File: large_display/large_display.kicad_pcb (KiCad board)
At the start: 2 copper layers, 128 parts, among them J1 Conn_01x11, J2 Conn_01x11, U1 TLC5940PWP

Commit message: routing: first pass done
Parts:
- removed R2: R, Resistor_SMD:R_0805_2012Metric_Pad1.15x1.40mm_HandSolder
- added REF**: MountingHole_3.2mm_M3, MountingHole:MountingHole_3.2mm_M3, F.Cu at (138.4, 146.8)
- added REF**: MountingHole_3.2mm_M3, MountingHole:MountingHole_3.2mm_M3, F.Cu at (54.0, 146.0)
- added REF**: MountingHole_3.2mm_M3, MountingHole:MountingHole_3.2mm_M3, F.Cu at (138.2, 53.8)
- added REF**: MountingHole_3.2mm_M3, MountingHole:MountingHole_3.2mm_M3, F.Cu at (53.7, 53.7)
- moved R35 18.8 mm to (120.8, 138.6)
- moved R1 17.2 mm to (138.0, 131.4)
- moved Dk5 17.2 mm to (100.5, 129.0)
- moved U1 17.1 mm to (131.9, 132.8)
- moved C1 17.1 mm to (134.5, 126.0)
- moved Dk4 17.1 mm to (97.3, 118.3)
- moved Dk2 17.0 mm to (98.9, 123.7)
- moved Dd5 16.9 mm to (97.4, 146.2)
- moved Da6 16.9 mm to (92.6, 54.3)
- moved Dd7 16.8 mm to (71.9, 146.2)
- moved De7 16.8 mm to (60.4, 135.1)
- moved Db5 16.8 mm to (116.3, 65.2)
- moved Dd2 16.8 mm to (91.0, 146.2)
- moved DL2 16.8 mm to (87.3, 116.9)
- moved DL5 16.8 mm to (87.7, 111.7)
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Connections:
- Df7 pad 1: Net-(Df7-Pad1) -> Net-(Df4-Pad1)
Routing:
- net Vdrive: track 0.00 -> 494.7 mm, vias 0 -> 22
- net Net-(Df4-Pad1): track 0.00 -> 148.1 mm, vias 0 -> 2
- net Net-(Da4-Pad1): track 0.00 -> 134.8 mm, vias 0 -> 6
- net Net-(J1-Pad7): track 0.00 -> 132.7 mm, vias 0 -> 2
- net Net-(Dg2-Pad1): track 0.00 -> 126.5 mm, vias 0 -> 4
- net Net-(Dn2-Pad1): track 0.00 -> 126.1 mm, vias 0 -> 6
- net Net-(J1-Pad8): track 0.00 -> 125.0 mm, vias 0 -> 2
- net VCC: track 0.00 -> 119.1 mm, vias 0 -> 4
- net Net-(J1-Pad6): track 0.00 -> 119.0 mm, vias 0 -> 2
- net Net-(J1-Pad5): track 0.00 -> 118.1 mm, vias 0 -> 2
- net Net-(J1-Pad3): track 0.00 -> 116.5 mm
- net Net-(J1-Pad2): track 0.00 -> 115.2 mm, vias 0 -> 2
- net Net-(J1-Pad1): track 0.00 -> 114.7 mm, vias 0 -> 2
- net Net-(J1-Pad4): track 0.00 -> 113.6 mm, vias 0 -> 2
- net Net-(Dh3-Pad1): track 0.00 -> 110.0 mm, vias 0 -> 6
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- added copper zone on B.Cu, net GND
- added copper zone on F.Cu, net GND
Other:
- board outline added: 92 x 100 mm
- net class Default: clearance 0.2 -> 0.16; trace_width 0.25 -> 0.2
- net class HiPower added: clearance 0.16, trace_width 0.6, via_dia 1, via_drill 0.5
- net class Lowpower added: clearance 0.16, trace_width 0.5, via_dia 1, via_drill 0.5
- rule trace_clearance: 0.2 -> 0.16
- board text added: "VLED GND VCC SDO SCK"

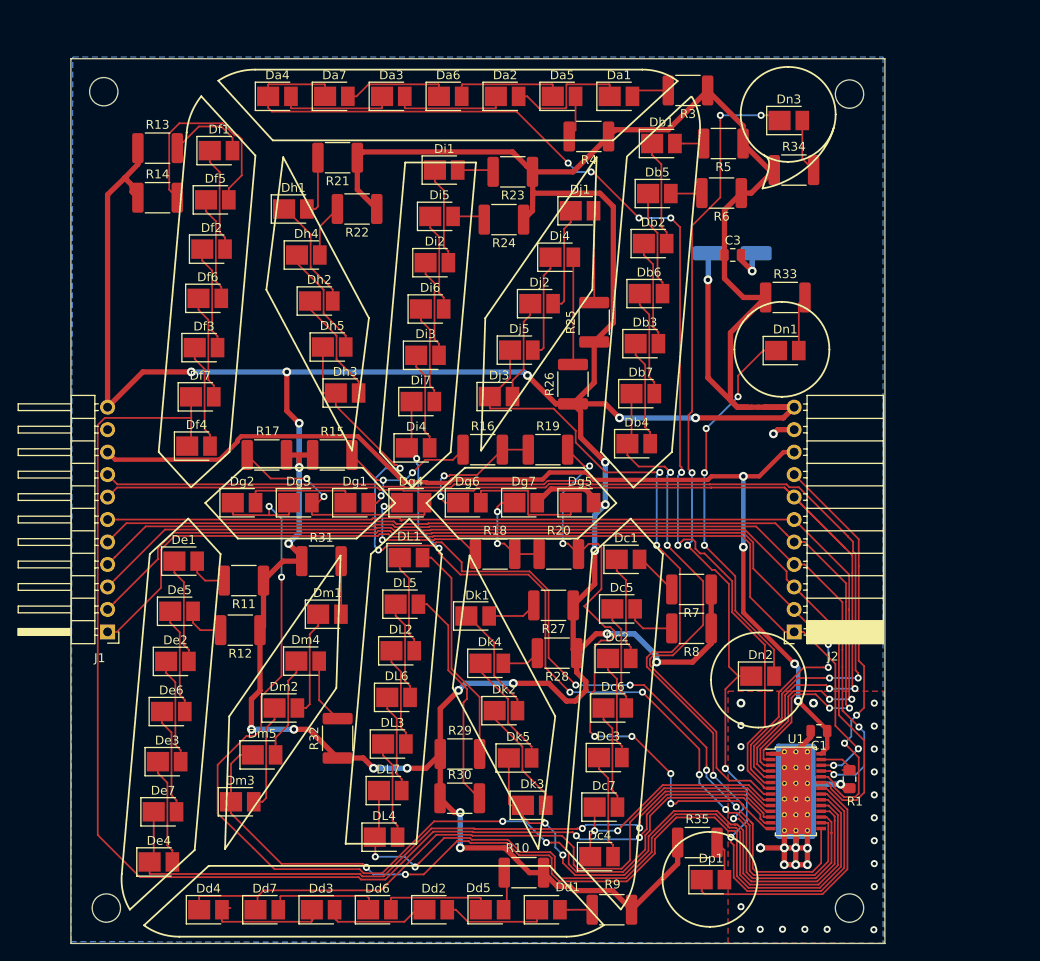
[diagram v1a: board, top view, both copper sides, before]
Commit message: first rev of layout done, text added to back silkscreen
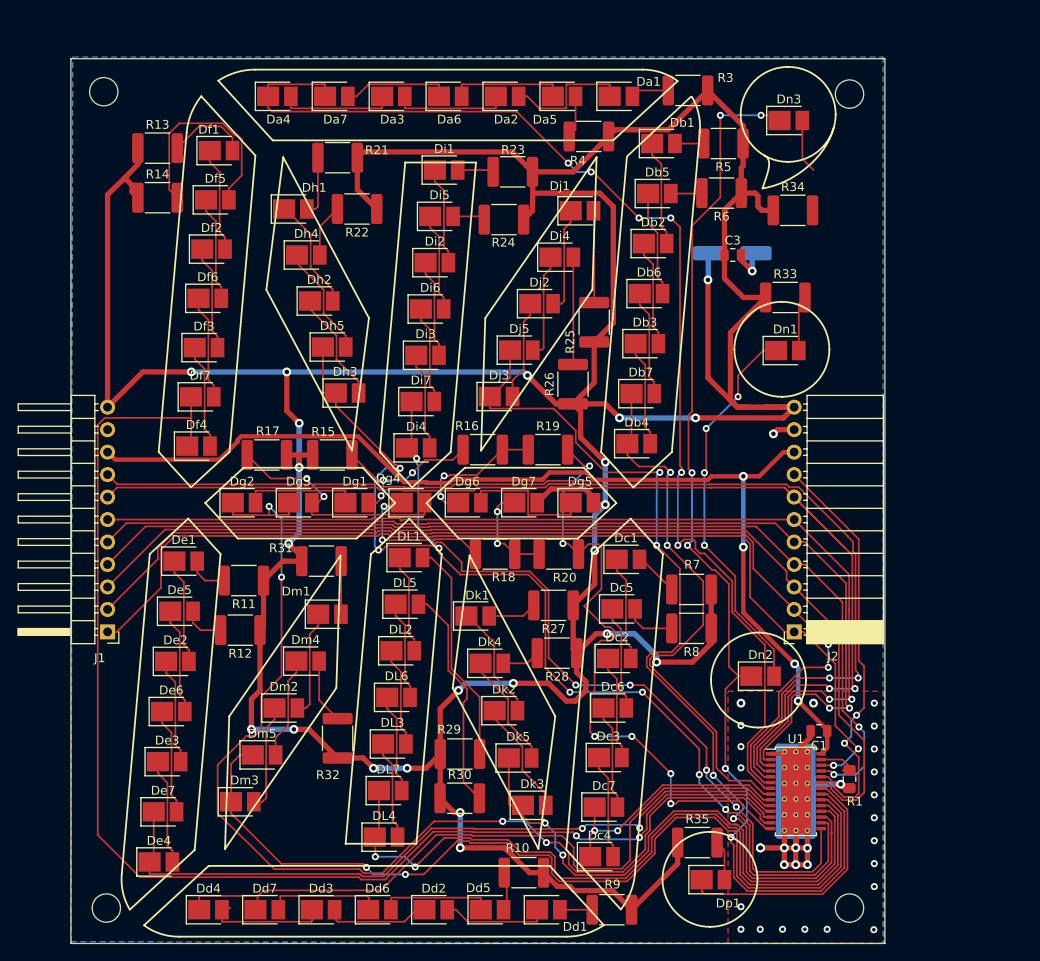
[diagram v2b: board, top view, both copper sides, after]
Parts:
- moved R34 4.55 mm to (131.6, 67.1)
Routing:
- net Vdrive: track 494.7 -> 495.9 mm
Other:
- board text added: "TLC5940 Output Mapping 0: a, 1: b, 2: c, 3: d 4: e, 5: f, 6: g, 7: g' 8: h, 9: i, 10: j, 11: k 12: L, 13: m, 14: n, 15, p R1 = 39/I(LED) e.g. R1 = 2k, I(LED) = 20mA 14 Segment DNF: R16, R18, Dg7 7 Segment DNF: Dh*, Di*, DJ*, Dk*, DL*, Dm* DNF: R15, R17, R19 - R32 Colon Fit: Dn1, Dn2, R33 Dec. Pt. Fit: Dp1, R35 Inv. Comma Fit: Dn3, R34"
- board text added: "VLED GND VCC SDIN SCLK XLAT BLANK GSCLK XERR VPRG DCPRG"
- board text added: "VLED GND VCC SDOUT SCLK XLAT BLANK GSCLK XERR VPRG DCPRG"
- board text removed: "VLED GND VCC SDO SCK"

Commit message: add url to silkscreen, add README, add licence
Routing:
- net Net-(Dn3-Pad2): track 6.13 -> 10.7 mm
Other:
- board text added: "TLC5940 Output Mapping 0: a, 1: b, 2: c, 3: d 4: e, 5: f, 6: g, 7: g' 8: h, 9: i, 10: j, 11: k 12: L, 13: m, 14: n, 15, p R1 = 39/I(LED) e.g. R1 = 2k, I(LED) = 20mA 14 Segment DNF: R16, R18, Dg7 7 Segment DNF: Dh*, Di*, DJ*, Dk*, DL*, Dm* DNF: R15, R17, R19 - R32 Colon Fit: Dn1, Dn2, R33 Dec. Pt. Fit: Dp1, R35 Inv. Comma Fit: Dn3, R34 https://github.com/nes0/large-display SPDX-License-Identifier: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"
- board text removed: "TLC5940 Output Mapping 0: a, 1: b, 2: c, 3: d 4: e, 5: f, 6: g, 7: g' 8: h, 9: i, 10: j, 11: k 12: L, 13: m, 14: n, 15, p R1 = 39/I(LED) e.g. R1 = 2k, I(LED) = 20mA 14 Segment DNF: R16, R18, Dg7 7 Segment DNF: Dh*, Di*, DJ*, Dk*, DL*, Dm* DNF: R15, R17, R19 - R32 Colon Fit: Dn1, Dn2, R33 Dec. Pt. Fit: Dp1, R35 Inv. Comma Fit: Dn3, R34"

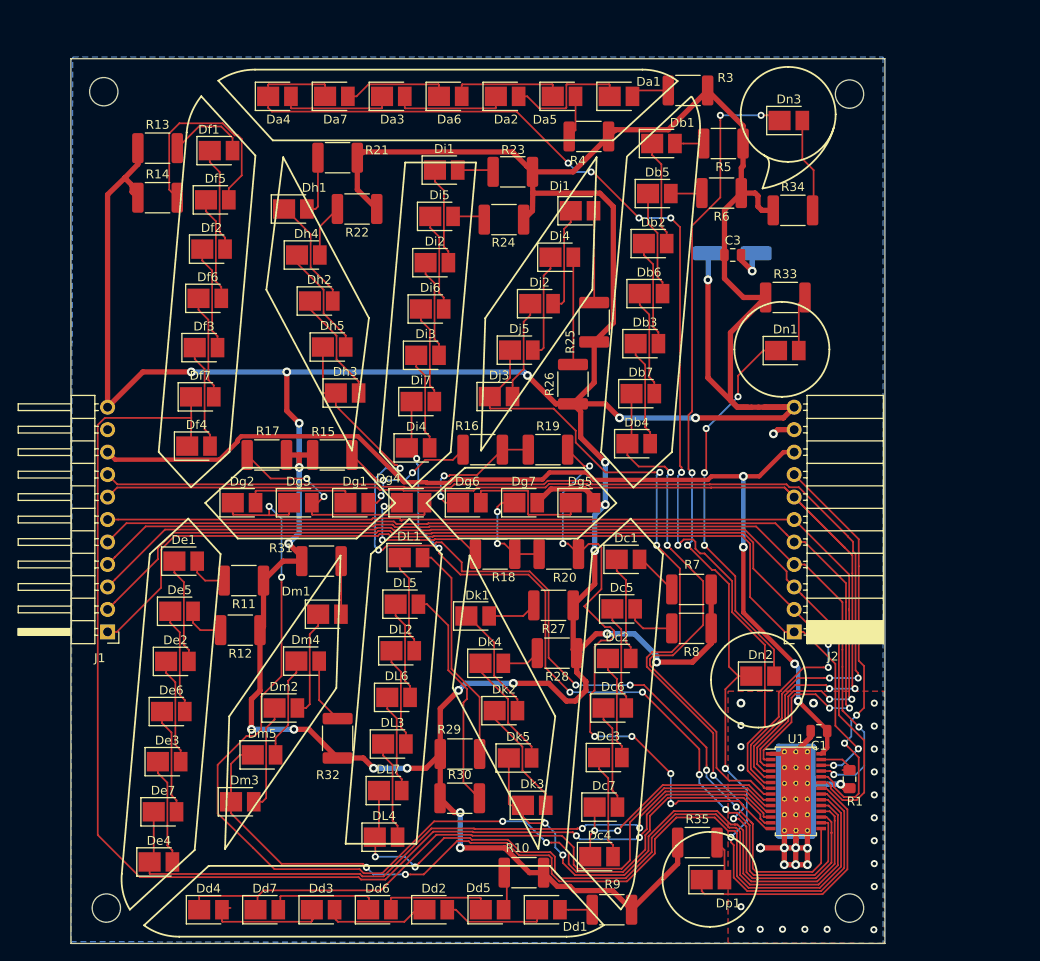
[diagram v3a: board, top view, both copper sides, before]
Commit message: Reverse Rg4 Reduce resistor size to 1206 Tidy up tracking Increase track width for VLED Fix text Add revision number
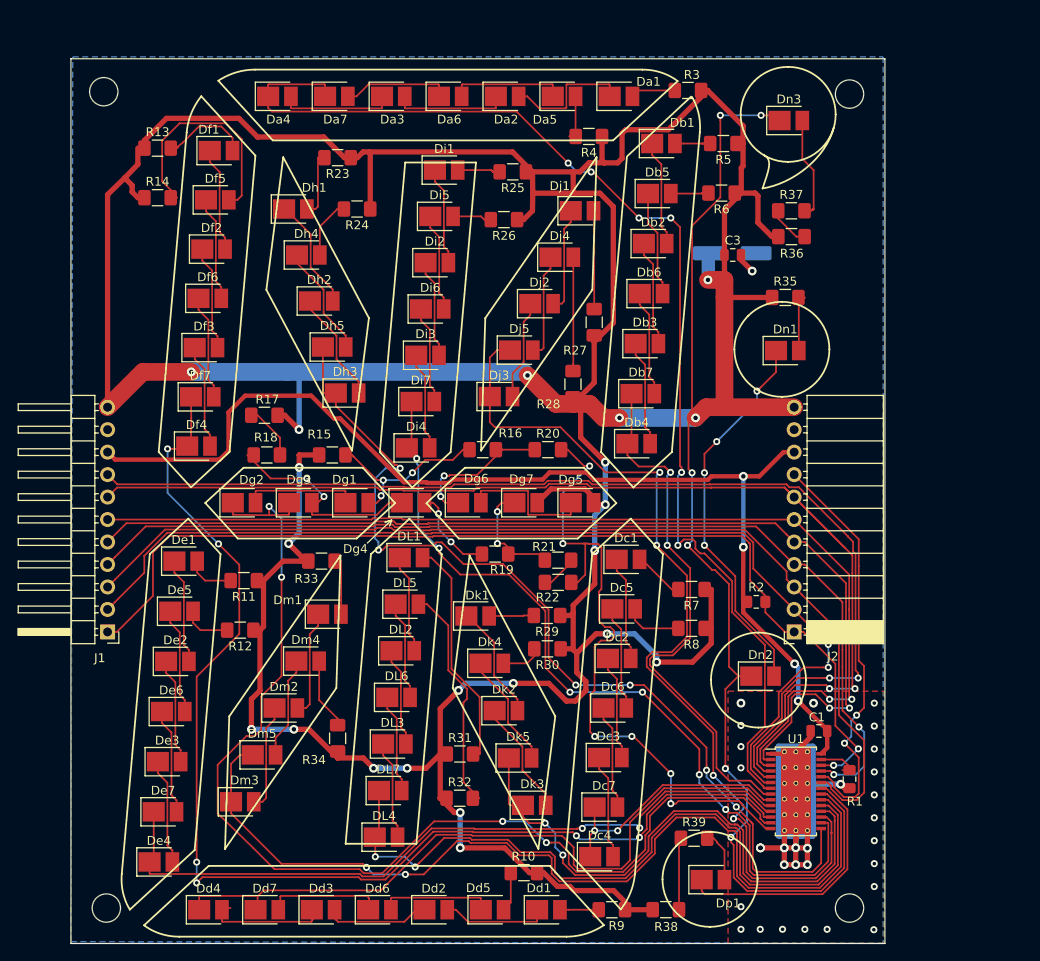
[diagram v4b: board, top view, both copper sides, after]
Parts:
- added R17: R, Resistor_SMD:R_1206_3216Metric_Pad1.42x1.75mm_HandSolder, F.Cu at (71.9, 90.3)
- added R2: 100k, Resistor_SMD:R_0805_2012Metric_Pad1.15x1.40mm_HandSolder, F.Cu at (127.5, 111.4)
- added R22: R, Resistor_SMD:R_1206_3216Metric_Pad1.42x1.75mm_HandSolder, F.Cu at (105.1, 109.2)
- added R37: R, Resistor_SMD:R_1206_3216Metric_Pad1.42x1.75mm_HandSolder, F.Cu at (131.4, 67.2)
- added R39: R, Resistor_SMD:R_1206_3216Metric_Pad1.42x1.75mm_HandSolder, F.Cu at (120.4, 138.1)
- C1, C3: value C -> 100n
- C2: value CP -> 10u
- R10, R11, R12, R13, R14, R15, R16, R3, R4, R5, R6, R7, R8, R9: footprint Resistor_SMD:R_1812_4532Metric_Pad1.30x3.40mm_HandSolder -> Resistor_SMD:R_1206_3216Metric_Pad1.42x1.75mm_HandSolder
- R18: renamed from R17; footprint Resistor_SMD:R_1812_4532Metric_Pad1.30x3.40mm_HandSolder -> Resistor_SMD:R_1206_3216Metric_Pad1.42x1.75mm_HandSolder
- R19: renamed from R18; footprint Resistor_SMD:R_1812_4532Metric_Pad1.30x3.40mm_HandSolder -> Resistor_SMD:R_1206_3216Metric_Pad1.42x1.75mm_HandSolder
- R20: renamed from R19; footprint Resistor_SMD:R_1812_4532Metric_Pad1.30x3.40mm_HandSolder -> Resistor_SMD:R_1206_3216Metric_Pad1.42x1.75mm_HandSolder
- R21: renamed from R20; footprint Resistor_SMD:R_1812_4532Metric_Pad1.30x3.40mm_HandSolder -> Resistor_SMD:R_1206_3216Metric_Pad1.42x1.75mm_HandSolder
- R23: renamed from R21; footprint Resistor_SMD:R_1812_4532Metric_Pad1.30x3.40mm_HandSolder -> Resistor_SMD:R_1206_3216Metric_Pad1.42x1.75mm_HandSolder
- R24: renamed from R22; footprint Resistor_SMD:R_1812_4532Metric_Pad1.30x3.40mm_HandSolder -> Resistor_SMD:R_1206_3216Metric_Pad1.42x1.75mm_HandSolder
- R25: renamed from R23; footprint Resistor_SMD:R_1812_4532Metric_Pad1.30x3.40mm_HandSolder -> Resistor_SMD:R_1206_3216Metric_Pad1.42x1.75mm_HandSolder
- R26: renamed from R24; footprint Resistor_SMD:R_1812_4532Metric_Pad1.30x3.40mm_HandSolder -> Resistor_SMD:R_1206_3216Metric_Pad1.42x1.75mm_HandSolder
- R27: renamed from R25; footprint Resistor_SMD:R_1812_4532Metric_Pad1.30x3.40mm_HandSolder -> Resistor_SMD:R_1206_3216Metric_Pad1.42x1.75mm_HandSolder
- R28: renamed from R26; footprint Resistor_SMD:R_1812_4532Metric_Pad1.30x3.40mm_HandSolder -> Resistor_SMD:R_1206_3216Metric_Pad1.42x1.75mm_HandSolder
- R29: renamed from R27; footprint Resistor_SMD:R_1812_4532Metric_Pad1.30x3.40mm_HandSolder -> Resistor_SMD:R_1206_3216Metric_Pad1.42x1.75mm_HandSolder
- R30: renamed from R28; footprint Resistor_SMD:R_1812_4532Metric_Pad1.30x3.40mm_HandSolder -> Resistor_SMD:R_1206_3216Metric_Pad1.42x1.75mm_HandSolder
- R31: renamed from R29; footprint Resistor_SMD:R_1812_4532Metric_Pad1.30x3.40mm_HandSolder -> Resistor_SMD:R_1206_3216Metric_Pad1.42x1.75mm_HandSolder
- R32: renamed from R30; footprint Resistor_SMD:R_1812_4532Metric_Pad1.30x3.40mm_HandSolder -> Resistor_SMD:R_1206_3216Metric_Pad1.42x1.75mm_HandSolder
- R33: renamed from R31; footprint Resistor_SMD:R_1812_4532Metric_Pad1.30x3.40mm_HandSolder -> Resistor_SMD:R_1206_3216Metric_Pad1.42x1.75mm_HandSolder
- R34: renamed from R32; footprint Resistor_SMD:R_1812_4532Metric_Pad1.30x3.40mm_HandSolder -> Resistor_SMD:R_1206_3216Metric_Pad1.42x1.75mm_HandSolder
- R35: renamed from R33; footprint Resistor_SMD:R_1812_4532Metric_Pad1.30x3.40mm_HandSolder -> Resistor_SMD:R_1206_3216Metric_Pad1.42x1.75mm_HandSolder
- R36: renamed from R34; footprint Resistor_SMD:R_1812_4532Metric_Pad1.30x3.40mm_HandSolder -> Resistor_SMD:R_1206_3216Metric_Pad1.42x1.75mm_HandSolder
- R38: renamed from R35; footprint Resistor_SMD:R_1812_4532Metric_Pad1.30x3.40mm_HandSolder -> Resistor_SMD:R_1206_3216Metric_Pad1.42x1.75mm_HandSolder
- moved R38 8.37 mm to (117.2, 146.2)
- moved R36 2.97 mm to (131.4, 70.1)
- moved R29 1.36 mm to (103.8, 112.9)
- moved R30 1.19 mm to (103.9, 116.7)
- moved R21 0.70 mm to (105.0, 106.7)
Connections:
- Dg4 pad 1: Net-(Dg4-Pad1) -> Net-(Dg3-Pad2)
- Dg4 pad 2: Net-(Dg3-Pad2) -> Net-(Dg4-Pad2)
- Dn2 pad 1: Net-(Dn2-Pad1) -> Vdrive
- Dn3 pad 1: Net-(Dn2-Pad1) -> Vdrive
- R18 pad 1: Vdrive -> Net-(R17-Pad2)
- R19 pad 1: Net-(Dg4-Pad1) -> Net-(Dg4-Pad2)
- R20 pad 2: Net-(R19-Pad2) -> Net-(R20-Pad2)
- R21 pad 2: Net-(R19-Pad2) -> Net-(R21-Pad2)
- R36 pad 2: Net-(Dn3-Pad2) -> Net-(R36-Pad2)
- R38 pad 2: Net-(Dp1-Pad2) -> Net-(R38-Pad2)
- U1 pad 14: Net-(R19-Pad2) -> Net-(R20-Pad2)
- U1 pad 21: Net-(Dn2-Pad1) -> Vdrive
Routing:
- net Vdrive: track 495.9 -> 641.1 mm, vias 22 -> 27
- net Net-(Dn2-Pad1): track 126.1 -> 0.00 mm, vias 6 -> 0
- net Net-(R20-Pad2): track 0.00 -> 75.0 mm, vias 0 -> 6
- net Net-(R19-Pad2): track 71.1 -> 0.00 mm, vias 6 -> 0
- net Net-(Dg4-Pad1): track 17.3 -> 0.00 mm, vias 2 -> 0
- net Net-(Df4-Pad1): track 148.1 -> 134.8 mm, vias 2 -> 6
- net Net-(Dg4-Pad2): track 0.00 -> 10.3 mm, vias 0 -> 2
- net Net-(R38-Pad2): track 0.00 -> 8.16 mm
- net VCC: track 119.1 -> 126.0 mm
- net Net-(R17-Pad2): track 0.00 -> 6.25 mm
- net Net-(R21-Pad2): track 0.00 -> 5.03 mm
- net Net-(R36-Pad2): track 0.00 -> 4.71 mm
- net GND: track 82.1 -> 78.0 mm, vias 32 -> 31
- net Net-(Dj3-Pad1): track 102.7 -> 105.6 mm
- net Net-(Dh3-Pad1): track 110.0 -> 108.1 mm
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
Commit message: Add buffering for passthru signals More tidying up of tracking
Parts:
- added U2: 74HC244, Package_SO:SSOP-20_5.3x7.2mm_P0.65mm, F.Cu at (56.2, 78.0)
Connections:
- Dn2 pad 1: Vdrive -> Net-(Dn2-Pad1)
- Dn3 pad 1: Vdrive -> Net-(Dn2-Pad1)
- J2 pad 1: Net-(J1-Pad1) -> Net-(J2-Pad1)
- J2 pad 4: Net-(J1-Pad4) -> Net-(J2-Pad4)
- J2 pad 5: Net-(J1-Pad5) -> Net-(J2-Pad5)
- J2 pad 6: Net-(J1-Pad6) -> Net-(J2-Pad6)
- J2 pad 7: Net-(J1-Pad7) -> Net-(J2-Pad7)
- R2 pad 2: Net-(J1-Pad1) -> Net-(J2-Pad1)
- U1 pad 2: Net-(J1-Pad5) -> Net-(J2-Pad5)
- U1 pad 21: Vdrive -> Net-(Dn2-Pad1)
- U1 pad 25: Net-(J1-Pad4) -> Net-(J2-Pad4)
- U1 pad 26: Net-(J1-Pad1) -> Net-(J2-Pad1)
- U1 pad 3: Net-(J1-Pad6) -> Net-(J2-Pad6)
- U1 pad 4: Net-(J1-Pad7) -> Net-(J2-Pad7)
- U1 pad 5: Net-(J1-Pad8) -> Net-(U1-Pad5)
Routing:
- net Net-(U1-Pad5): track 0.00 -> 162.0 mm, vias 0 -> 2
- net Net-(J2-Pad7): track 0.00 -> 158.3 mm, vias 0 -> 2
- net Net-(J2-Pad6): track 0.00 -> 151.9 mm, vias 0 -> 2
- net Net-(J2-Pad5): track 0.00 -> 148.1 mm, vias 0 -> 2
- net Net-(J2-Pad4): track 0.00 -> 146.7 mm, vias 0 -> 4
- net Vdrive: track 641.1 -> 500.6 mm, vias 27 -> 22
- net Net-(J2-Pad1): track 0.00 -> 140.3 mm, vias 0 -> 4
- net Net-(Dn2-Pad1): track 0.00 -> 128.8 mm, vias 0 -> 6
- net Net-(J1-Pad7): track 132.7 -> 34.8 mm, vias 2 -> 0
- net Net-(J1-Pad8): track 125.0 -> 31.9 mm, vias 2 -> 0
- net Net-(J1-Pad4): track 113.6 -> 27.2 mm, vias 2 -> 0
- net Net-(J1-Pad6): track 118.7 -> 40.0 mm, vias 2 -> 0
- net Net-(J1-Pad1): track 115.0 -> 38.6 mm, vias 2 -> 0
- net Net-(J1-Pad5): track 118.1 -> 45.5 mm, vias 2 -> 0
- net VCC: track 126.0 -> 158.7 mm, vias 4 -> 7
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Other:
- net class Default: clearance 0.16 -> 0.14
- net class HiPower: clearance 0.16 -> 0.14
- net class Lowpower: clearance 0.16 -> 0.14
- rule trace_clearance: 0.16 -> 0.14
- board text added: "TLC5940 Output Mapping 0: a, 1: b, 2: c, 3: d 4: e, 5: f, 6: g, 7: g' 8: h, 9: i, 10: j, 11: k 12: L, 13: m, 14: n, 15, p R1 = 39/I(LED) e.g. R1 = 2k, I(LED) = 20mA 14 Segment DNF: R16, R19, Dg4 7 Segment DNF: Dh*, Di*, DJ*, Dk*, DL*, Dm* DNF: R15, R17-18, R20-39 Colon Fit: Dn1, Dn2, R33 Dec. Pt. Fit: Dp1, R35 Inv. Comma Fit: Dn3, R34 rev 0.2 https://github.com/nes0/large-display SPDX-License-Ide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"
- board text removed: "TLC5940 Output Mapping 0: a, 1: b, 2: c, 3: d 4: e, 5: f, 6: g, 7: g' 8: h, 9: i, 10: j, 11: k 12: L, 13: m, 14: n, 15, p R1 = 39/I(LED) e.g. R1 = 2k, I(LED) = 20mA 14 Segment DNF: R16, R18, Dg7 7 Segment DNF: Dh*, Di*, DJ*, Dk*, DL*, Dm* DNF: R15, R17, R19 - R32 Colon Fit: Dn1, Dn2, R33 Dec. Pt. Fit: Dp1, R35 Inv. Comma Fit: Dn3, R34 https://github.com/nes0/large-display SPDX-License-Identifier: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"

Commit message: add decoupling for buffer IC
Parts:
- added C4: 100n, Capacitor_SMD:C_0805_2012Metric, F.Cu at (57.4, 85.3)
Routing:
- net Net-(J2-Pad4): track 146.7 -> 141.9 mm
- net VCC: track 158.7 -> 162.8 mm
- net GND: track 89.9 -> 93.6 mm
- net Net-(J1-Pad1): track 38.6 -> 41.7 mm
- net Net-(J2-Pad1): track 140.3 -> 139.6 mm
